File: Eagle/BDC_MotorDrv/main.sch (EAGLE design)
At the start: 28 parts, among them U1 ATTINY10-TSHR

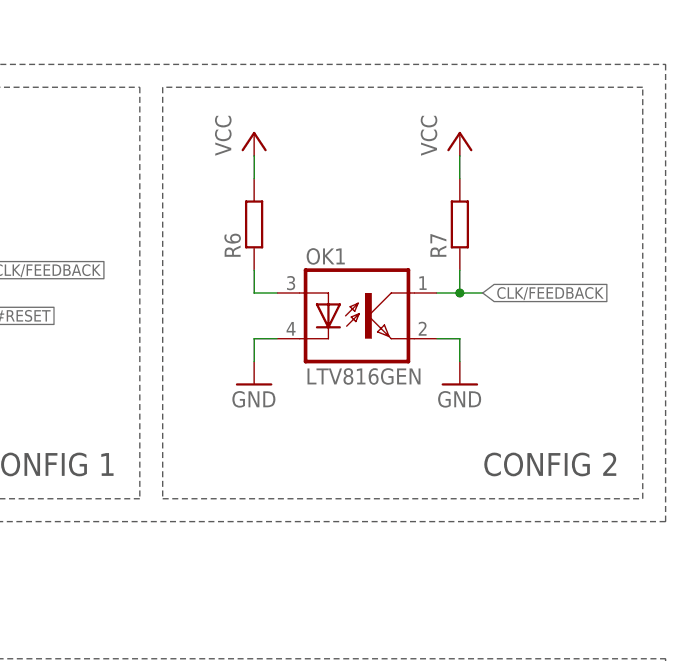
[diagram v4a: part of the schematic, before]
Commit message: Removed redundant feedback optocoupler
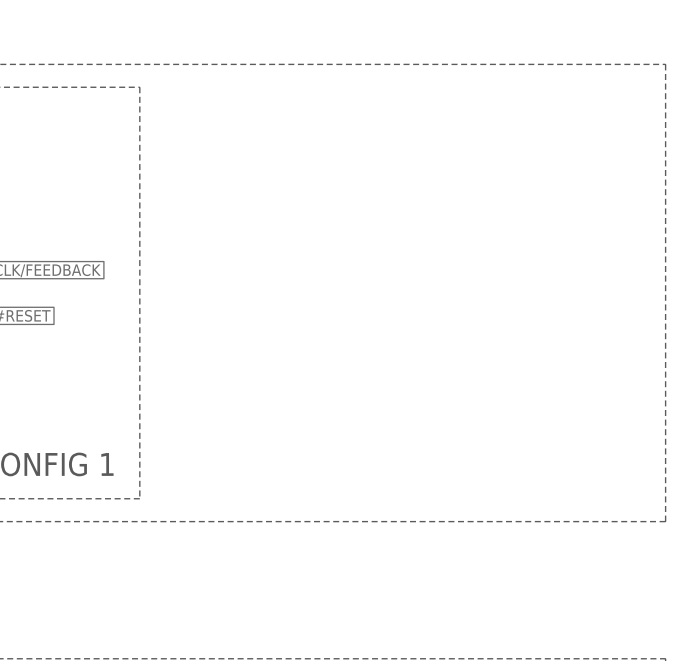
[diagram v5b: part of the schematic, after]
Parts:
- removed OK1: LTV816GEN, optocoupler:LTV816GEN
- removed R6, R7: (no value), rcl:R-EU_R0603
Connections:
- removed net N$2: OK1.A, R6.1
- net CLK/FEEDBACK: no longer OK1.COL, R7.1
- net GND: no longer OK1.C, OK1.EMIT
- net VCC: no longer R6.2, R7.2
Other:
- note removed: "CONFIG 2"
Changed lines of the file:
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@@
 <part name="P+6" library="supply1" deviceset="VCC" device=""/>
 <part name="GND4" library="supply1" deviceset="GND" device=""/>
-<part name="P+7" library="supply1" deviceset="VCC" device=""/>
-<part name="GND5" library="supply1" deviceset="GND" device=""/>
 <part name="OK2" library="optocoupler" deviceset="LTV816" device="S"/>
-<part name="OK1" library="optocoupler" deviceset="LTV816" device="GEN"/>
-<part name="R6" library="rcl" deviceset="R-EU_" device="R0603"/>
-<part name="R7" library="rcl" deviceset="R-EU_" device="R0603"/>
-<part name="P+8" library="supply1" deviceset="VCC" device=""/>
-<part name="GND6" library="supply1" deviceset="GND" device=""/>
 <part name="PAD6" library="wirepad" deviceset="WIREPAD" device="SMD1,27-254"/>
 <part name="PAD7" library="wirepad" deviceset="WIREPAD" device="SMD1,27-254"/>
@@
 <wire x1="142.24" y1="50.8" x2="81.28" y2="50.8" width="0.1524" layer="97" style="shortdash"/>
 <wire x1="81.28" y1="50.8" x2="81.28" y2="96.52" width="0.1524" layer="97" style="shortdash"/>
-<wire x1="144.78" y1="96.52" x2="144.78" y2="50.8" width="0.1524" layer="97" style="shortdash"/>
-<wire x1="144.78" y1="50.8" x2="198.12" y2="50.8" width="0.1524" layer="97" style="shortdash"/>
-<wire x1="198.12" y1="50.8" x2="198.12" y2="96.52" width="0.1524" layer="97" style="shortdash"/>
-<wire x1="198.12" y1="96.52" x2="144.78" y2="96.52" width="0.1524" layer="97" style="shortdash"/>
 <text x="124.46" y="53.34" size="2.54" layer="97">CONFIG 1</text>
-<text x="180.34" y="53.34" size="2.54" layer="97">CONFIG 2</text>
 <wire x1="119.38" y1="30.48" x2="198.12" y2="30.48" width="0.1524" layer="97" style="shortdash"/>
 <wire x1="198.12" y1="30.48" x2="198.12" y2="-35.56" width="0.1524" layer="97" style="shortdash"/>
@@
 <instance part="P+6" gate="VCC" x="88.9" y="86.36"/>
 <instance part="GND4" gate="1" x="88.9" y="63.5"/>
-<instance part="P+7" gate="VCC" x="154.94" y="91.44"/>
-<instance part="GND5" gate="1" x="154.94" y="63.5"/>
 <instance part="OK2" gate="G$1" x="149.86" y="0"/>
-<instance part="OK1" gate="G$1" x="167.64" y="71.12"/>
-<instance part="R6" gate="G$1" x="154.94" y="81.28" rot="R90"/>
-<instance part="R7" gate="G$1" x="177.8" y="81.28" rot="R90"/>
-<instance part="P+8" gate="VCC" x="177.8" y="91.44"/>
-<instance part="GND6" gate="1" x="177.8" y="63.5"/>
 <instance part="PAD6" gate="G$1" x="48.26" y="-20.32"/>
 <instance part="PAD7" gate="G$1" x="48.26" y="-25.4"/>
@@
 <wire x1="96.52" y1="81.28" x2="88.9" y2="81.28" width="0.1524" layer="91"/>
 <junction x="88.9" y="81.28"/>
-</segment>
-<segment>
-<pinref part="P+7" gate="VCC" pin="VCC"/>
-<pinref part="R6" gate="G$1" pin="2"/>
-<wire x1="154.94" y1="88.9" x2="154.94" y2="86.36" width="0.1524" layer="91"/>
-</segment>
-<segment>
-<pinref part="R7" gate="G$1" pin="2"/>
-<pinref part="P+8" gate="VCC" pin="VCC"/>
-<wire x1="177.8" y1="86.36" x2="177.8" y2="88.9" width="0.1524" layer="91"/>
 </segment>
 </net>
@@
 <junction x="88.9" y="68.58"/>
 </segment>
-<segment>
-<pinref part="OK1" gate="G$1" pin="C"/>
-<pinref part="GND5" gate="1" pin="GND"/>
-<wire x1="157.48" y1="68.58" x2="154.94" y2="68.58" width="0.1524" layer="91"/>
-<wire x1="154.94" y1="68.58" x2="154.94" y2="66.04" width="0.1524" layer="91"/>
-</segment>
-<segment>
-<pinref part="OK1" gate="G$1" pin="EMIT"/>
-<wire x1="175.26" y1="68.58" x2="177.8" y2="68.58" width="0.1524" layer="91"/>
-<wire x1="177.8" y1="68.58" x2="177.8" y2="66.04" width="0.1524" layer="91"/>
-<pinref part="GND6" gate="1" pin="GND"/>
-</segment>
 </net>
 <net name="N$10" class="0">
@@
 </segment>
 <segment>
-<pinref part="R7" gate="G$1" pin="1"/>
-<pinref part="OK1" gate="G$1" pin="COL"/>
-<wire x1="177.8" y1="76.2" x2="177.8" y2="73.66" width="0.1524" layer="91"/>
-<wire x1="177.8" y1="73.66" x2="175.26" y2="73.66" width="0.1524" layer="91"/>
-<wire x1="177.8" y1="73.66" x2="180.34" y2="73.66" width="0.1524" layer="91"/>
-<junction x="177.8" y="73.66"/>
-<label x="180.34" y="73.66" size="1.27" layer="95" xref="yes"/>
-</segment>
-<segment>
 <pinref part="PAD8" gate="G$1" pin="P"/>
 <wire x1="55.88" y1="-30.48" x2="50.8" y2="-30.48" width="0.1524" layer="91"/>
@@
 </segment>
 </net>
-<net name="N$2" class="0">
-<segment>
-<pinref part="OK1" gate="G$1" pin="A"/>
-<pinref part="R6" gate="G$1" pin="1"/>
-<wire x1="157.48" y1="73.66" x2="154.94" y2="73.66" width="0.1524" layer="91"/>
-<wire x1="154.94" y1="73.66" x2="154.94" y2="76.2" width="0.1524" layer="91"/>
-</segment>
-</net>
